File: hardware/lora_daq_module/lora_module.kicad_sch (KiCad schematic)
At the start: 35 parts, among them J2 SMA_Edge_50Ω, J3 USB_C_Receptacle_USB2.0_14P, J4 EXT_UART, J5 SWD, J6 Micro_SD_Card_Det1, U3 CP2102N-Axx-xQFN20, U4 Wio-E5_STM32WLE5JC, U5 CAT24C256

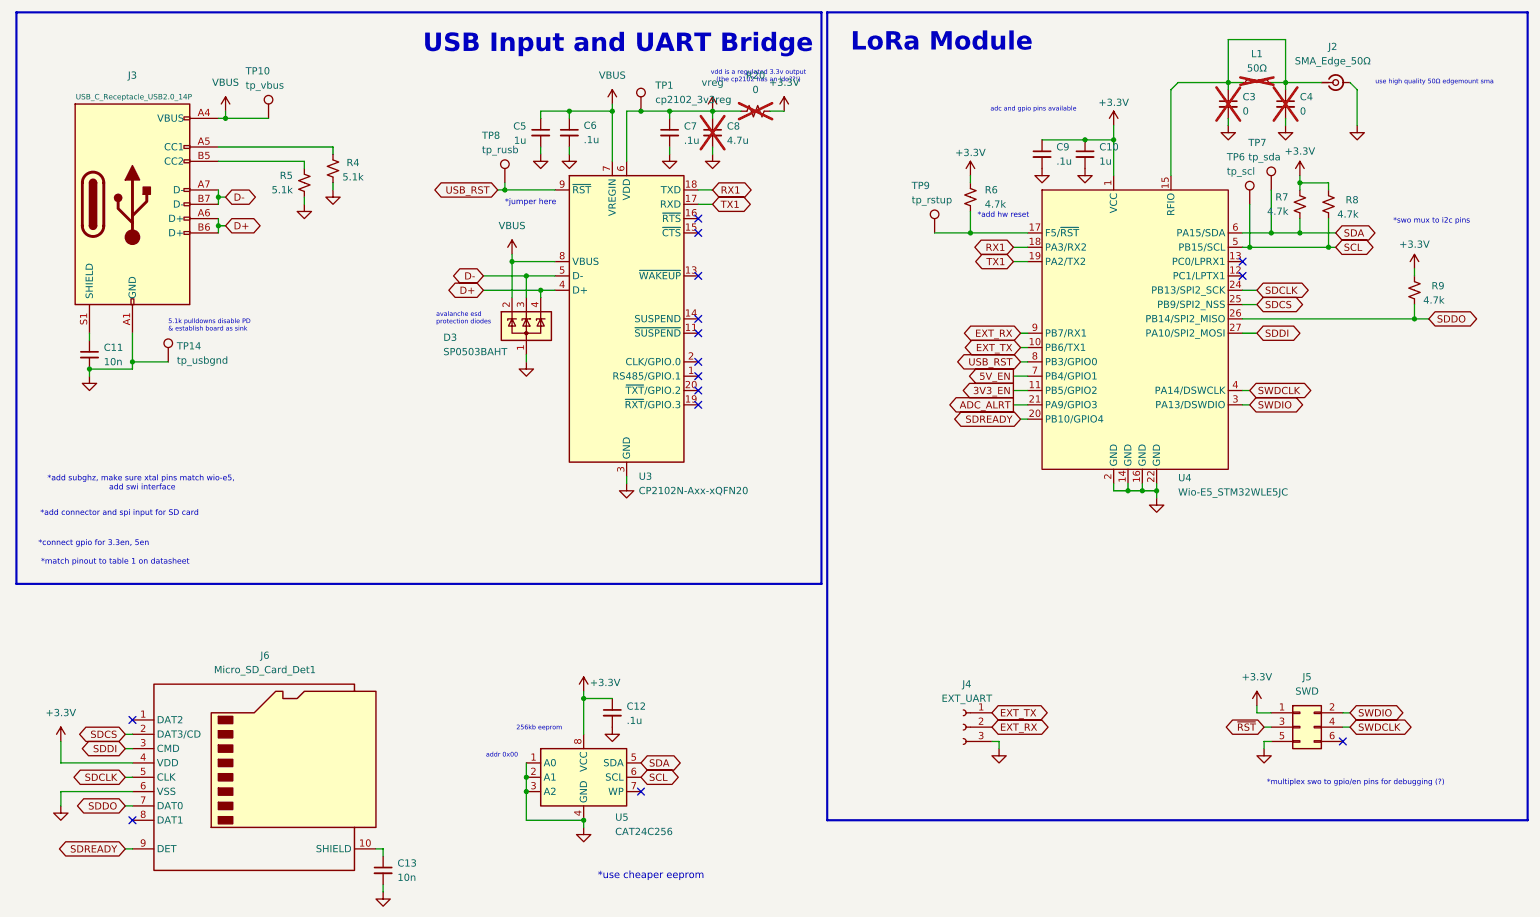
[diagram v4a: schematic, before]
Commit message: add 0Ω resistors for disabling power circuits, revise adc input buffer and filter based on design review feedback, revise microstrip trace, add hardware reset button, add i2c connector and jst receptacle for battery
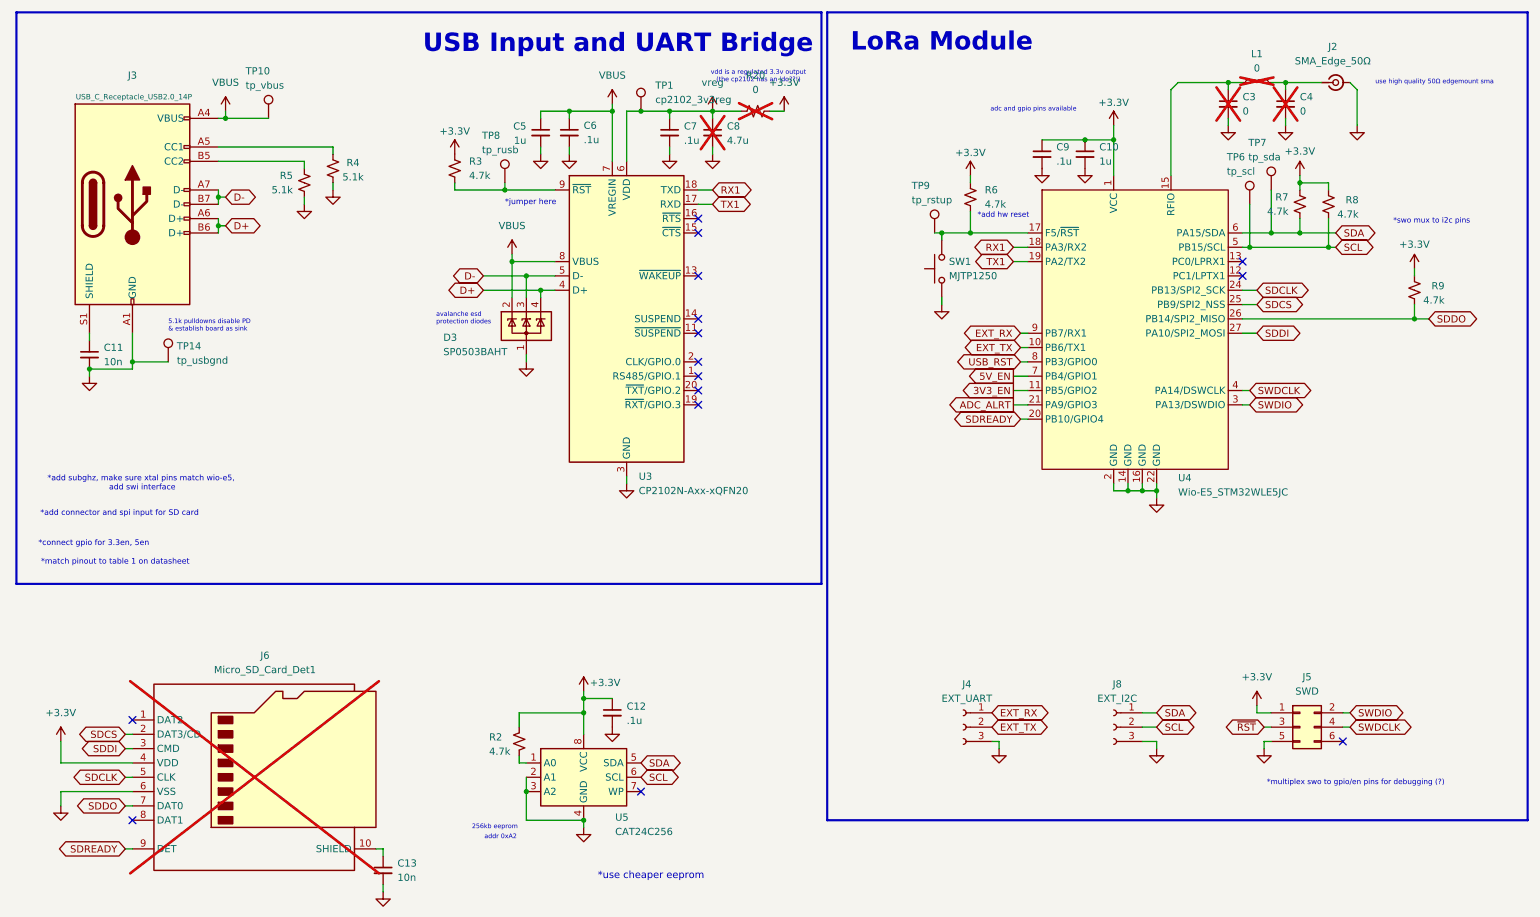
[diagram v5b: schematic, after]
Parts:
- added J8: EXT_I2C, Connector_JST:JST_EH_B3B-EH-A_1x03_P2.50mm_Vertical, symbol Connector:Conn_01x03_Socket
- added R2, R3: 4.7k, Resistor_SMD:R_0603_1608Metric, symbol Device:R_Small_US
- added SW1: MJTP1250, Button_Switch_THT:SW_PUSH_1P1T_6x3.5mm_H5.0_APEM_MJTP1250, symbol Switch:SW_Push
- C3, C4: footprint Capacitor_SMD:C_0603_1608Metric -> Capacitor_SMD:C_0402_1005Metric
- C8: Desc (none) -> 4.7 µF ±10% 50V Ceramic Capacitor X7R 1206 (3216 Metric); Dist (none) -> Digikey; Dist PN (none) -> 490-6521-1-ND; Mfr (none) -> Murata Electronics; Mfr PN (none) -> GRM31CR71H475KA12L
- J6: now not fitted
- L1: value 50Ω -> 0; footprint Resistor_SMD:R_0603_1608Metric -> Inductor_SMD:L_0402_1005Metric; Desc 50 Ohms ±0.1% 0.52W Chip Resistor 1206 (3216 Metric) Anti-S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 -> 0 Ohms Jumper Chip Resistor 0402 (1005 Metric) Moisture Res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; Dist PN 541-TNPW120650R0BEENCT-ND -> 311-0.0JRCT-ND; Mfr Vishay Dale -> YAGEO; Mfr PN TNPW120650R0BEEN -> RC0402JR-070RL; now in the parts list
- R20: Desc (none) -> 0 Ohms Jumper Chip Resistor 0603 (1608 Metric) Automotive A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; Dist (none) -> Digikey; Dist PN (none) -> RMCF0603ZT0R00CT-ND; Mfr (none) -> Stackpole Electronics Inc; Mfr PN (none) -> RMCF0603ZT0R00
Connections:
- net +3.3V: now also R2.2, R3.1
- net EXT_RX: now also J4.1 (Pin_1); no longer J4.2 (Pin_2)
- net EXT_TX: now also J4.2 (Pin_2); no longer J4.1 (Pin_1)
- net GND: now also J8.3 (Pin_3), SW1.1; no longer U5.1 (A0)
- net SCL: now also J8.2 (Pin_2)
- net SDA: now also J8.1 (Pin_1)
- net USB_RST: no longer TP8.1, U3.9 (~{RST})
- net at C4.1, J2.1 (In), L1.2: no longer C3.1, L1.1, U4.15 (RFIO)
- net at R6.2, TP9.1, U4.17 (F5/~{RST}): now also SW1.2
- new net: R3.2, TP8.1, U3.9 (~{RST})
- new net: C3.1, L1.1, U4.15 (RFIO)
- new net: R2.1, U5.1 (A0)
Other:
- note added: "addr 0xA2"
- note removed: "addr 0x00"
